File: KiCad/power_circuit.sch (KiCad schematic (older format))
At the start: 17 parts

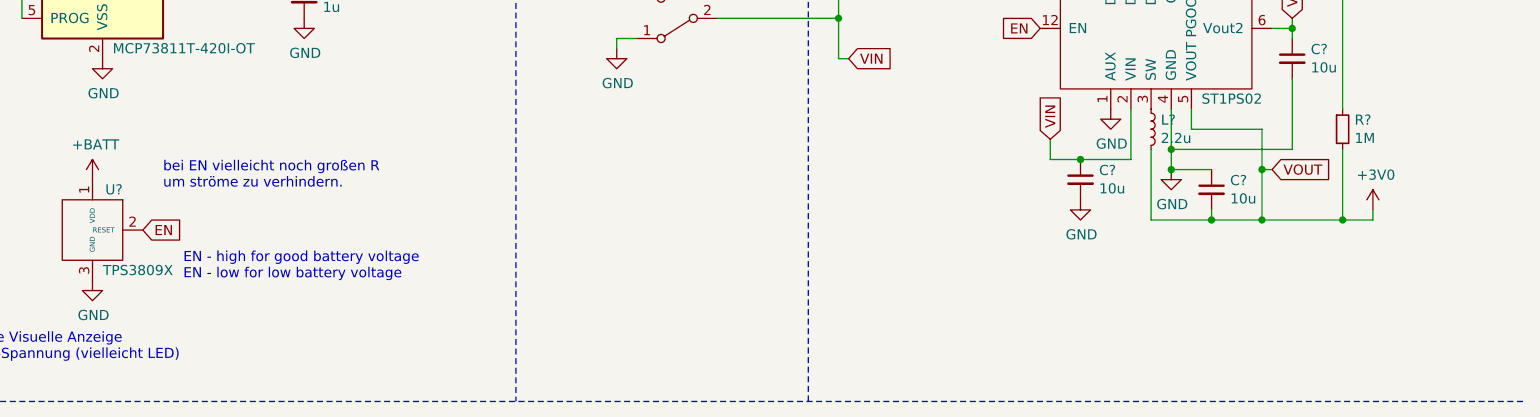
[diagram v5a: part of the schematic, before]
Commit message: kleines Kommentar angepasst
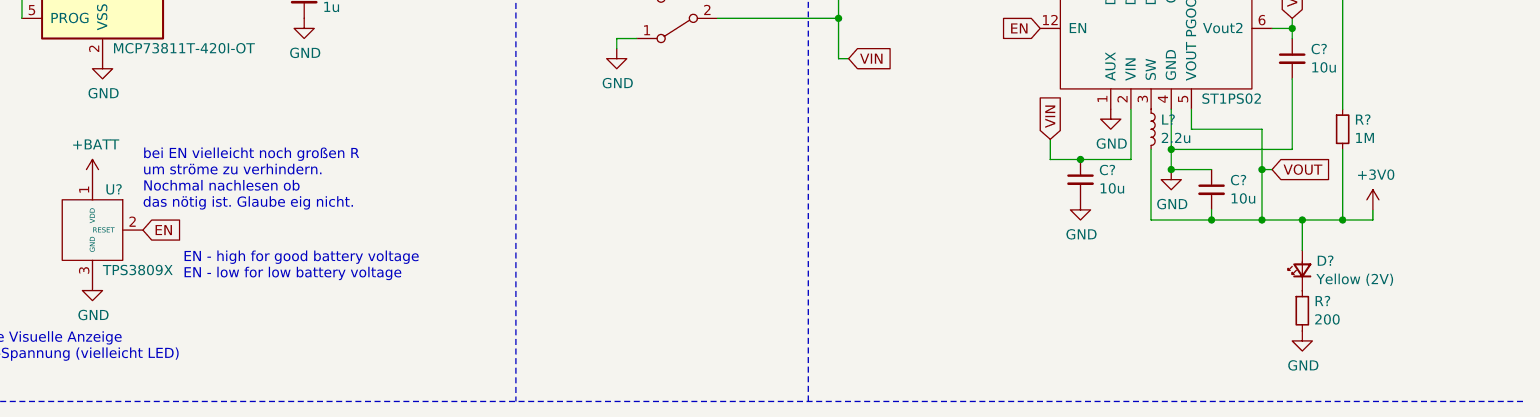
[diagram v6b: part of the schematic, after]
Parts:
- added D?: Yellow (2V), symbol Device:LED_Small
- added R?: 200, symbol Device:R_Small
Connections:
- net +3V0: now also D?.2 (A)
- net GND: now also R?.2
- new net: D?.1 (K), R?.1
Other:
- note added: "bei EN vielleicht noch großen R\num ströme zu verhindern.\nNochmal nachlesen ob\ndas nötig ist. Glaube eig nicht."
- note removed: "bei EN vielleicht noch großen R\num ströme zu verhindern."
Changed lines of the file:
@@
 	10300 3750 10300 4100
 Wire Wire Line
-	10300 4100 9900 4100
+	10300 4100 10100 4100
 Connection ~ 9900 4100
 Wire Wire Line
@@
 Text Notes 3050 4800 0    50   ~ 0
 Es fehlt noch eine Visuelle Anzeige\nfür geringe Akku-Spannung (vielleicht LED)
-Text Notes 4450 3950 0    50   ~ 0
-bei EN vielleicht noch großen R\num ströme zu verhindern.
+Text Notes 4350 4050 0    50   ~ 0
+bei EN vielleicht noch großen R\num ströme zu verhindern.\nNochmal nachlesen ob\ndas nötig ist. Glaube eig nicht.
+$Comp
+L Device:LED_Small D?
+U 1 1 608B6AC0
+P 10100 4350
+F 0 "D?" V 10146 4280 50  0000 R CNN
+F 1 "Yellow (2V)" V 10055 4280 50  0000 R CNN
+F 2 "" V 10100 4350 50  0001 C CNN
+F 3 "~" V 10100 4350 50  0001 C CNN
+	1    10100 4350
+	0    -1   -1   0
+$EndComp
+$Comp
+L Device:R_Small R?
+U 1 1 608B6DF2
+P 10100 4550
+F 0 "R?" H 10159 4596 50  0000 L CNN
+F 1 "200" H 10159 4505 50  0000 L CNN
+F 2 "" H 10100 4550 50  0001 C CNN
+F 3 "~" H 10100 4550 50  0001 C CNN
+	1    10100 4550
+	1    0    0    -1
+$EndComp
+$Comp
+L power:GND #PWR?
+U 1 1 608B722A
+P 10100 4650
+F 0 "#PWR?" H 10100 4400 50  0001 C CNN
+F 1 "GND" H 10105 4477 50  0000 C CNN
+F 2 "" H 10100 4650 50  0001 C CNN
+F 3 "" H 10100 4650 50  0001 C CNN
+	1    10100 4650
+	1    0    0    -1
+$EndComp
+Wire Wire Line
+	10100 4250 10100 4100
+Connection ~ 10100 4100
+Wire Wire Line
+	10100 4100 9900 4100
 $EndSCHEMATC

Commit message: paar Sachen mit Manu angepasst
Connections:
- net +BATT: now also C?.1, U?.11 (D2), U?.2 (VIN)
- net EN: now also SW?.2 (B)
- removed net D2: C?.1, SW?.2 (B), U?.11 (D2), U?.2 (VIN)
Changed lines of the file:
@@
 D0, D1 low and D2 high for 3.0V output
 Wire Wire Line
-	7800 3300 7850 3300
-Wire Wire Line
-	7800 3100 7800 3300
-Wire Wire Line
-	7800 2900 7850 2900
-Connection ~ 7800 3100
-Wire Wire Line
-	7800 3100 7800 2900
-Text GLabel 7850 2900 2    50   Input ~ 0
+	8250 2450 8300 2450
+Text GLabel 8300 2450 2    50   Input ~ 0
 D2
-Text GLabel 7850 3300 2    50   Input ~ 0
+Text GLabel 8350 3600 2    50   Input ~ 0
 VIN
 $Comp
@@
 Wire Wire Line
 	10100 4100 9900 4100
+$Comp
+L power:+BATT #PWR?
+U 1 1 608C855C
+P 8250 2450
+AR Path="/608C855C" Ref="#PWR?"  Part="1"
+AR Path="/608A57BF/608C855C" Ref="#PWR?"  Part="1"
+F 0 "#PWR?" H 8250 2300 50  0001 C CNN
+F 1 "+BATT" H 8265 2623 50  0000 C CNN
+F 2 "" H 8250 2450 50  0001 C CNN
+F 3 "" H 8250 2450 50  0001 C CNN
+	1    8250 2450
+	1    0    0    -1
+$EndComp
+Text GLabel 7800 3100 2    50   Input ~ 0
+EN
+$Comp
+L power:+BATT #PWR?
+U 1 1 608C8BB8
+P 8250 3500
+AR Path="/608C8BB8" Ref="#PWR?"  Part="1"
+AR Path="/608A57BF/608C8BB8" Ref="#PWR?"  Part="1"
+F 0 "#PWR?" H 8250 3350 50  0001 C CNN
+F 1 "+BATT" H 8265 3673 50  0000 C CNN
+F 2 "" H 8250 3500 50  0001 C CNN
+F 3 "" H 8250 3500 50  0001 C CNN
+	1    8250 3500
+	1    0    0    -1
+$EndComp
+Wire Wire Line
+	8250 3500 8250 3600
+Wire Wire Line
+	8250 3600 8350 3600
 $EndSCHEMATC
